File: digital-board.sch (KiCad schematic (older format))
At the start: 233 parts, among them IC1 ATMEGA6450-A, J1 CONN_20X2, Q1 2N3904, Q2 2N3904, SW15 TACT_SWITCH, SW16 TACT_SWITCH, SW17 TACT_SWITCH, SW18 TACT_SWITCH, SW19 TACT_SWITCH, SW20 TACT_SWITCH, SW21 TACT_SWITCH, SW22 TACT_SWITCH, SW23 TACT_SWITCH, U1 DG419, U10 74LVC1G32, U11 74HC165, U12 74AC595, U13 74AC595, U14 74HC165, U15 74AC595, U16 74AC595, U2 74HC4067, U3 R-78E5.0-1.0, U4 74HC4067, U5 74LS573, U6 74LS573, U7 74LVC2G04, U8 74AC595, U9 74HC165, X1 MIDI OUT, X2 MIDI IN, X3 MIDI THRU

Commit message: routing
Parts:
- removed C18: 0.1µ, ~, symbol C_US
- removed U11: 74HC165, symbol 74HC165
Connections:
- net labels added: ISW10, ISW11, ISW8, ISW9, SW21, SW22
- wire segments 829 -> 804
- no-connect marks 27 -> 26
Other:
- moved on the sheet: R53, TP9, VR16, VR17, VR18

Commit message: just before first ses import
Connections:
- wire segments 804 -> 802
- no-connect marks 26 -> 28
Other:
- moved on the sheet: LED1, R4
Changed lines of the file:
@@
 L LED LED1
 U 1 1 54587D7E
-P 7500 6450
-F 0 "LED1" H 7500 6550 50  0000 C CNN
-F 1 "LED" H 7500 6350 50  0000 C CNN
-F 2 "~" H 7500 6450 60  0000 C CNN
-F 3 "~" H 7500 6450 60  0000 C CNN
-	1    7500 6450
+P 7600 4300
+F 0 "LED1" H 7600 4400 50  0000 C CNN
+F 1 "LED" H 7600 4200 50  0000 C CNN
+F 2 "~" H 7600 4300 60  0000 C CNN
+F 3 "~" H 7600 4300 60  0000 C CNN
+	1    7600 4300
 	0    1    1    0
 $EndComp
@@
 L R_US R4
 U 1 1 54587D84
-P 7500 6050
-F 0 "R4" V 7580 6050 50  0000 C CNN
-F 1 "330" V 7420 6050 50  0000 C CNN
-F 2 "" H 7500 6050 60  0000 C CNN
-F 3 "" H 7500 6050 60  0000 C CNN
-	1    7500 6050
+P 7600 3900
+F 0 "R4" V 7680 3900 50  0000 C CNN
+F 1 "330" V 7520 3900 50  0000 C CNN
+F 2 "" H 7600 3900 60  0000 C CNN
+F 3 "" H 7600 3900 60  0000 C CNN
+	1    7600 3900
 	-1   0    0    1
 $EndComp
@@
 L GND_E #PWR02
 U 1 1 54587D8A
-P 7500 6650
-F 0 "#PWR02" V 7500 6650 30  0001 C CNN
-F 1 "GND_E" H 7500 6580 30  0001 C CNN
-F 2 "~" H 7500 6650 60  0000 C CNN
-F 3 "~" H 7500 6650 60  0000 C CNN
-	1    7500 6650
+P 7600 4500
+F 0 "#PWR02" V 7600 4500 30  0001 C CNN
+F 1 "GND_E" H 7600 4430 30  0001 C CNN
+F 2 "~" H 7600 4500 60  0000 C CNN
+F 3 "~" H 7600 4500 60  0000 C CNN
+	1    7600 4500
 	1    0    0    -1
 $EndComp
@@
 Connection ~ 7250 12150
 Wire Wire Line
-	7500 5700 7500 5850
+	7600 3550 7600 3700
 Wire Wire Line
 	3550 4950 2250 4950
@@
 	2700 12350 2700 12600
 Wire Wire Line
-	6150 5700 7500 5700
-Wire Wire Line
 	3550 4650 3350 4650
 Wire Wire Line
@@
 	9950 8050 9950 8300
 Wire Wire Line
-	6150 3550 6250 3550
-Wire Wire Line
 	6150 3450 6250 3450
 Wire Wire Line
@@
 NoConn ~ 3550 2950
 NoConn ~ 3550 3050
-NoConn ~ 6250 3550
+NoConn ~ 6150 5700
 NoConn ~ 6250 2950
 $Comp
@@
 Wire Wire Line
 	3450 5700 3550 5700
+NoConn ~ 7600 3550
+NoConn ~ 6150 3550
 $EndSCHEMATC

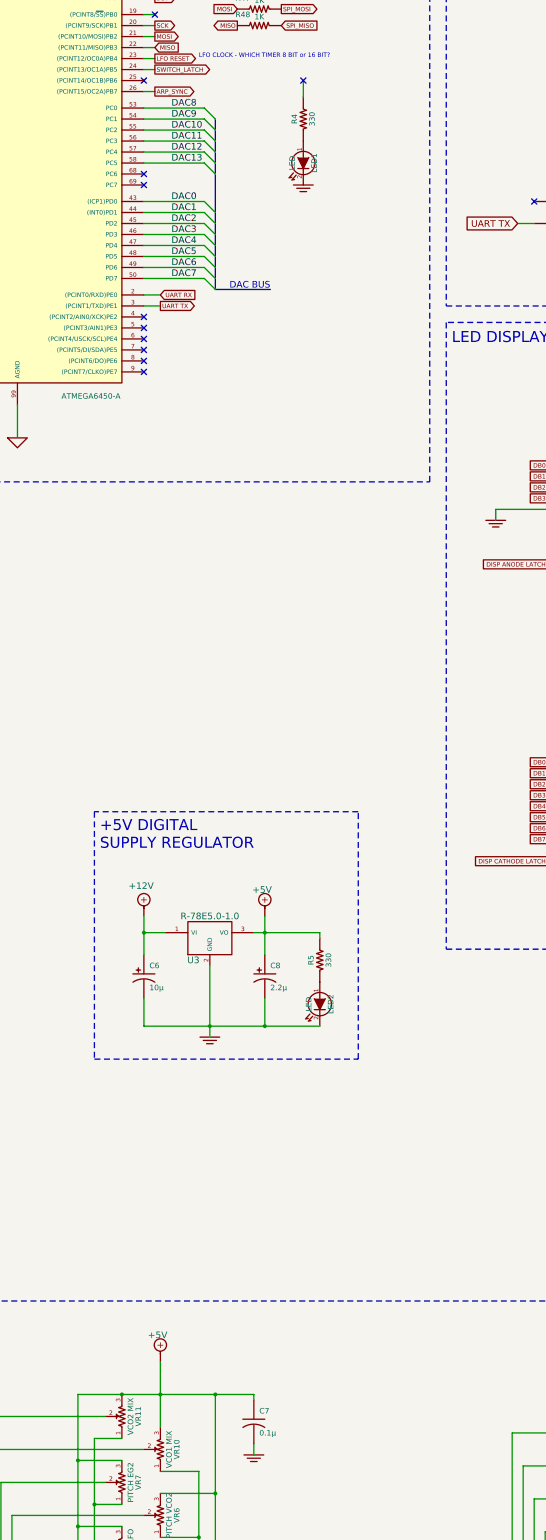
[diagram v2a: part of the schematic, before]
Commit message: main routing done. touch ups, adding decoupling
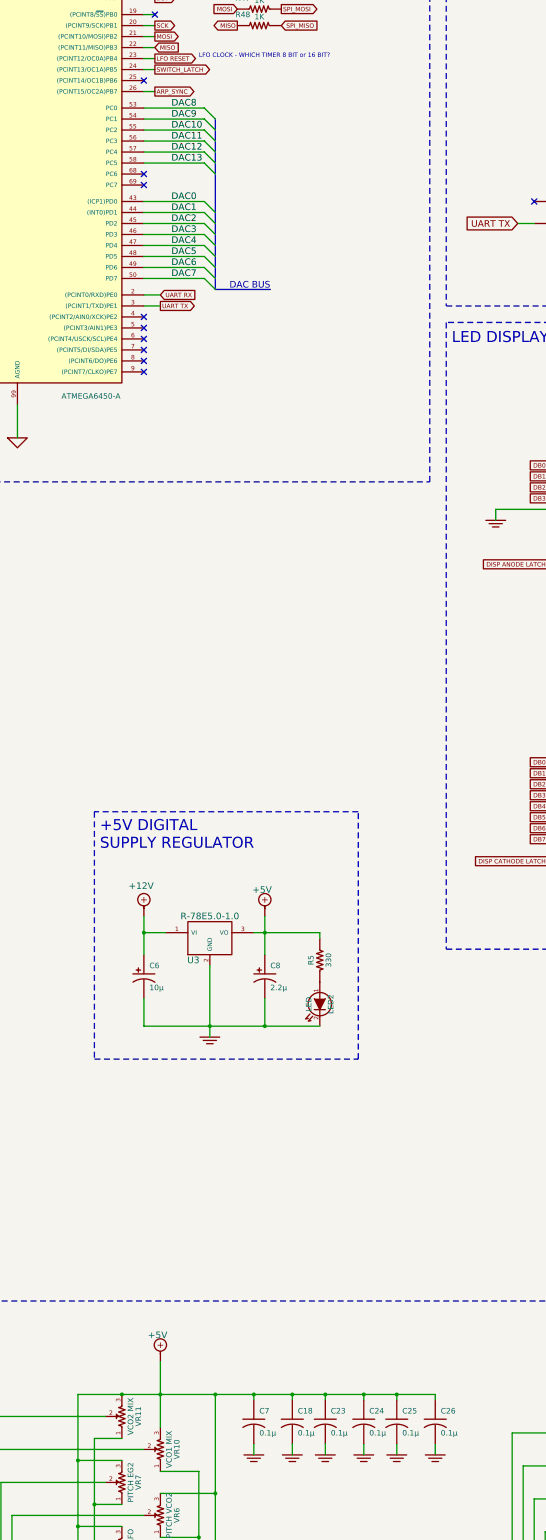
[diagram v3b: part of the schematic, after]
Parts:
- removed LED1: LED, ~, symbol LED
- removed R4: 330, symbol R_US
- added C18, C23, C24, C25, C26: 0.1µ, ~, symbol C_US
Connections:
- wire segments 802 -> 811
- no-connect marks 28 -> 27

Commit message: GND test points added, more silkscreen work
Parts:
- added TP1, TP2: CONN_1, symbol CONN_1
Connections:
- wire segments 811 -> 813
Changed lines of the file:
@@
 	24650 17550 24650 17700
-Wire Wire Line
-	22700 17950 23650 17950
 Wire Wire Line
 	26600 18650 26600 18750
@@
 	8800 15500 8800 15550
 Connection ~ 8450 15500
+$Comp
+L CONN_1 TP1
+U 1 1 54DAE206
+P 7600 10500
+F 0 "TP1" V 7750 10450 60  0000 L CNN
+F 1 "CONN_1" H 7600 10555 30  0001 C CNN
+F 2 "" H 7600 10500 60  0000 C CNN
+F 3 "" H 7600 10500 60  0000 C CNN
+	1    7600 10500
+	0    -1   -1   0
+$EndComp
+$Comp
+L GND_E #PWR0116
+U 1 1 54DAFB61
+P 7600 10800
+F 0 "#PWR0116" V 7600 10800 30  0001 C CNN
+F 1 "GND_E" H 7600 10730 30  0001 C CNN
+F 2 "~" H 7600 10800 60  0000 C CNN
+F 3 "~" H 7600 10800 60  0000 C CNN
+	1    7600 10800
+	1    0    0    -1
+$EndComp
+Wire Wire Line
+	7600 10650 7600 10800
+Wire Wire Line
+	22900 17950 23650 17950
+$Comp
+L CONN_1 TP2
+U 1 1 54DB9950
+P 7900 10500
+F 0 "TP2" V 8050 10450 60  0000 L CNN
+F 1 "CONN_1" H 7900 10555 30  0001 C CNN
+F 2 "" H 7900 10500 60  0000 C CNN
+F 3 "" H 7900 10500 60  0000 C CNN
+	1    7900 10500
+	0    -1   -1   0
+$EndComp
+$Comp
+L GND_E #PWR?
+U 1 1 54DB9956
+P 7900 10800
+F 0 "#PWR?" V 7900 10800 30  0001 C CNN
+F 1 "GND_E" H 7900 10730 30  0001 C CNN
+F 2 "~" H 7900 10800 60  0000 C CNN
+F 3 "~" H 7900 10800 60  0000 C CNN
+	1    7900 10800
+	1    0    0    -1
+$EndComp
+Wire Wire Line
+	7900 10650 7900 10800
 $EndSCHEMATC

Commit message: more silkscreen work almost ready to order
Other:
- note added: "Changed from \n+12V to +5V\nTESTED"
- note removed: "Changed from \n+12V to +5V\nneed to test this!"
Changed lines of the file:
@@
 $EndComp
 Text Notes 14550 19250 0    60   ~ 0
-Changed from \n+12V to +5V\nneed to test this!
+Changed from \n+12V to +5V\nTESTED
 Wire Notes Line
 	15150 19500 14600 19500

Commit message: spi_en added to all 595s
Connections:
- wire segments 813 -> 809
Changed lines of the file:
@@
 ~SPI_EN
-$Comp
-L GND_E #PWR073
-U 1 1 54B969CA
-P 15400 6050
-F 0 "#PWR073" V 15400 6050 30  0001 C CNN
-F 1 "GND_E" H 15400 5980 30  0001 C CNN
-F 2 "~" H 15400 6050 60  0000 C CNN
-F 3 "~" H 15400 6050 60  0000 C CNN
-	1    15400 6050
-	1    0    0    -1
-$EndComp
-$Comp
-L GND_E #PWR074
-U 1 1 54B9BFF4
-P 15350 13400
-F 0 "#PWR074" V 15350 13400 30  0001 C CNN
-F 1 "GND_E" H 15350 13330 30  0001 C CNN
-F 2 "~" H 15350 13400 60  0000 C CNN
-F 3 "~" H 15350 13400 60  0000 C CNN
-	1    15350 13400
-	1    0    0    -1
-$EndComp
-$Comp
-L GND_E #PWR075
-U 1 1 54B9CA20
-P 15350 17100
-F 0 "#PWR075" V 15350 17100 30  0001 C CNN
-F 1 "GND_E" H 15350 17030 30  0001 C CNN
-F 2 "~" H 15350 17100 60  0000 C CNN
-F 3 "~" H 15350 17100 60  0000 C CNN
-	1    15350 17100
-	1    0    0    -1
-$EndComp
-$Comp
-L GND_E #PWR076
-U 1 1 54BA1724
-P 15350 9750
-F 0 "#PWR076" V 15350 9750 30  0001 C CNN
-F 1 "GND_E" H 15350 9680 30  0001 C CNN
-F 2 "~" H 15350 9750 60  0000 C CNN
-F 3 "~" H 15350 9750 60  0000 C CNN
-	1    15350 9750
-	1    0    0    -1
-$EndComp
 $Comp
 L 74HC165 U14
@@
 	15100 6200 15600 6200
 Wire Wire Line
-	15600 5950 15400 5950
-Wire Wire Line
-	15400 5950 15400 6050
-Wire Wire Line
-	15550 13300 15350 13300
-Wire Wire Line
-	15350 13300 15350 13400
-Wire Wire Line
-	15550 17000 15350 17000
-Wire Wire Line
-	15350 17000 15350 17100
-Wire Wire Line
 	17000 7850 15100 7850
 Wire Wire Line
@@
 Wire Wire Line
 	15100 9900 15550 9900
-Wire Wire Line
-	15550 9650 15350 9650
-Wire Wire Line
-	15350 9650 15350 9750
 Wire Wire Line
 	16950 11550 15050 11550
@@
 Wire Wire Line
 	7900 10650 7900 10800
+Text GLabel 15500 5950 0    40   Input ~ 0
+~SPI_EN
+Wire Wire Line
+	15600 5950 15500 5950
+Text GLabel 15500 9650 0    40   Input ~ 0
+~SPI_EN
+Wire Wire Line
+	15500 9650 15550 9650
+Text GLabel 15500 13300 0    40   Input ~ 0
+~SPI_EN
+Wire Wire Line
+	15550 13300 15500 13300
+Text GLabel 15450 17000 0    40   Input ~ 0
+~SPI_EN
+Wire Wire Line
+	15450 17000 15550 17000
 $EndSCHEMATC

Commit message: ready to order
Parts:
- C8: value 2.2µ -> 10µF
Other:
- note added: "SPI_EN added to all 595s\nto keep LEDs off during\nMCU boot"
- note removed: "THIS ENABLE IS OF QUESTIONABLE USE\nTO STOP LEDS\nFROM BLINKING\nDURING MCU BOOT\nNEED EN/PULLUP\nON ALL 595s"
